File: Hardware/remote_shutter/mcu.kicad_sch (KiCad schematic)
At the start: 27 parts, among them J4 Buzzer, U2 ESP32-PICO-MINI-02, Y1 NX3215SA-32.768K-STD-MUA-14

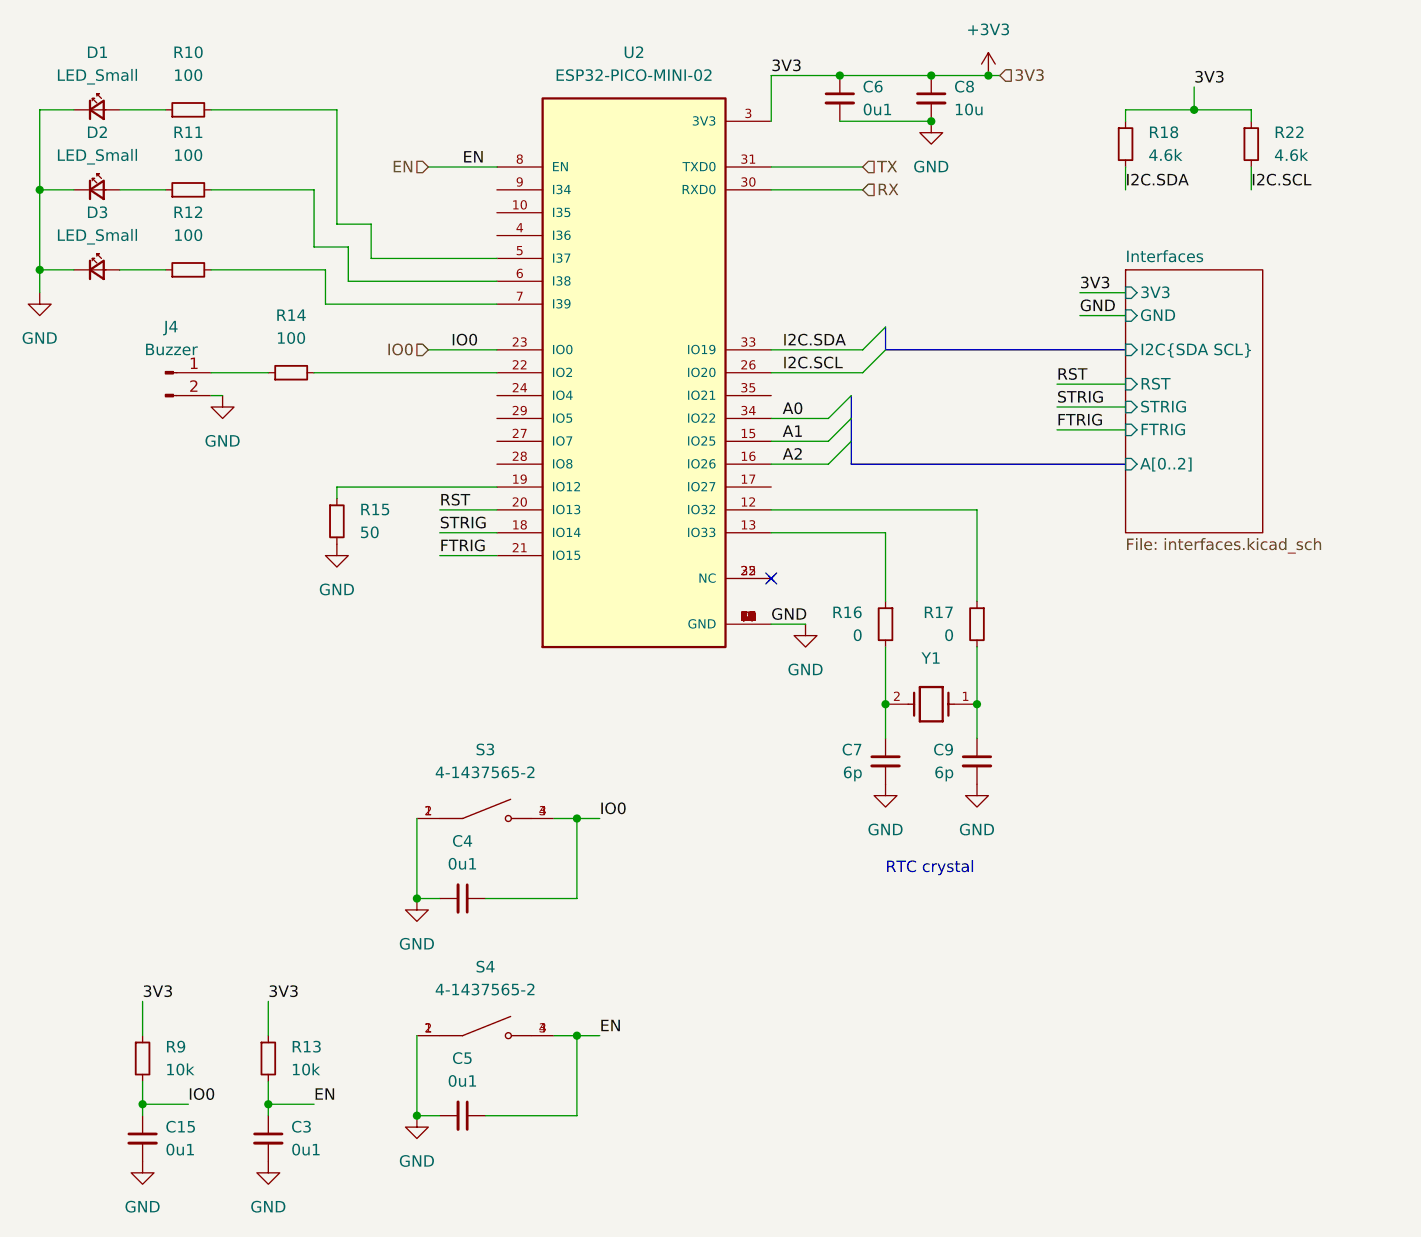
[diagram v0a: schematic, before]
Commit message: Added debug connectors
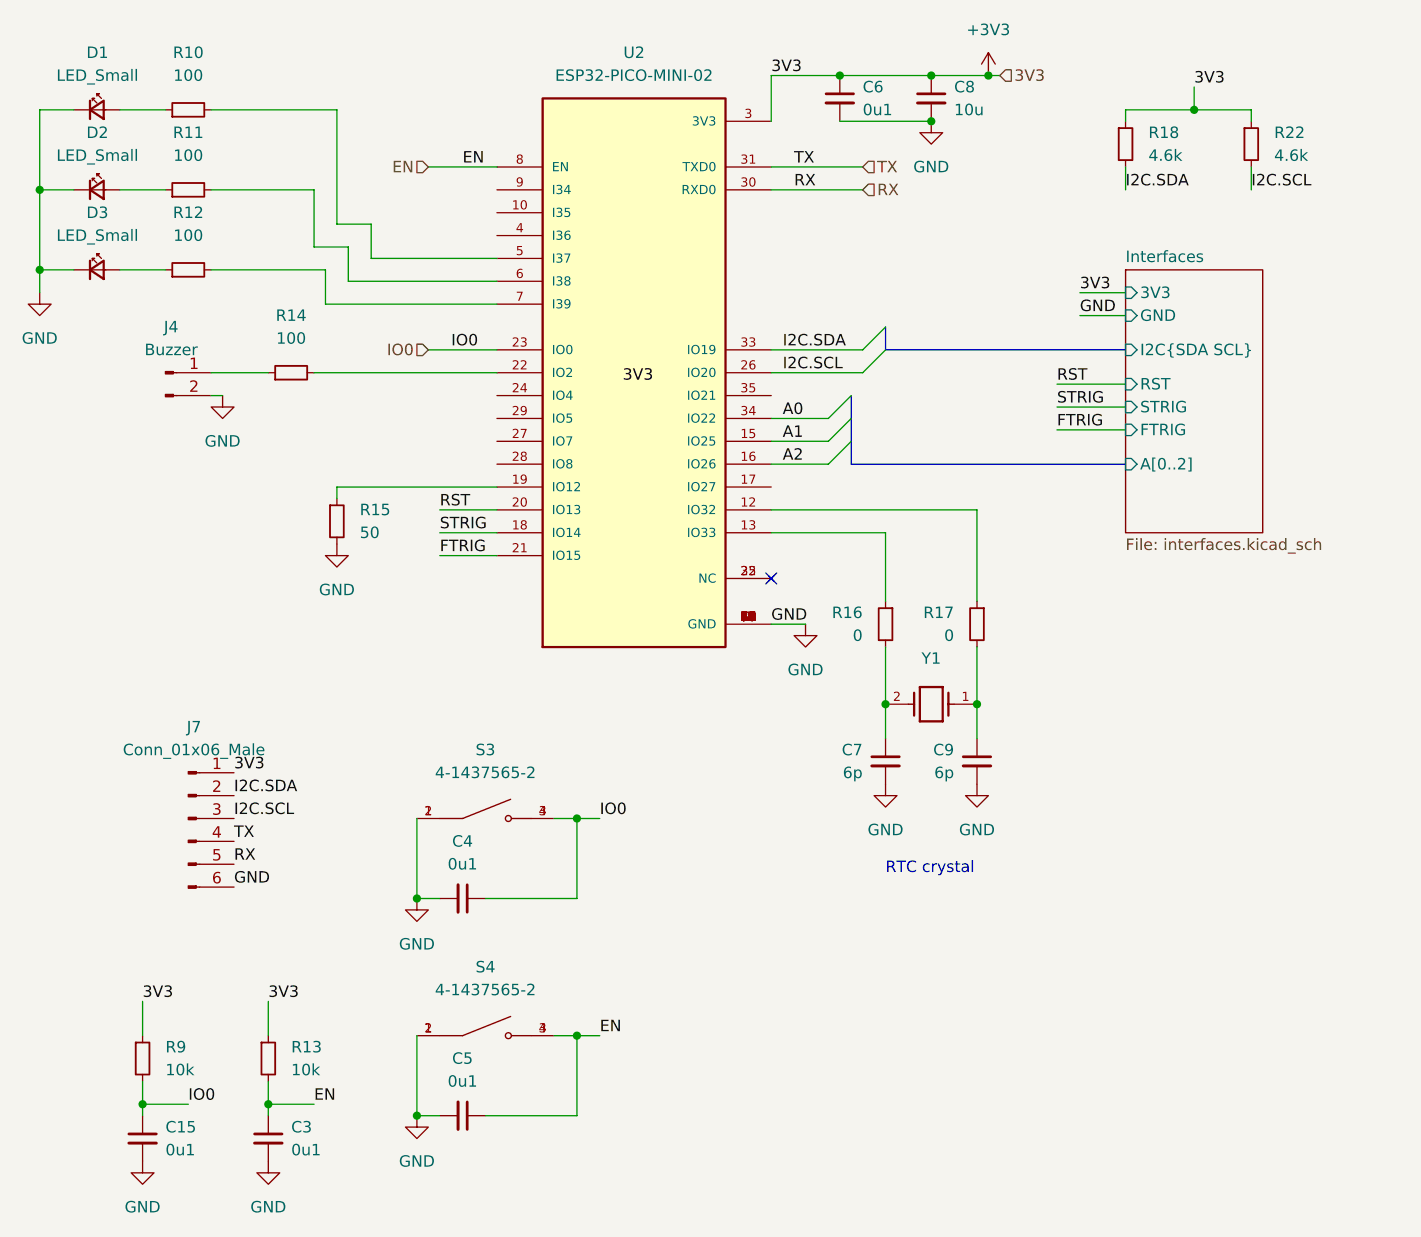
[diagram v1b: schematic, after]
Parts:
- added J7: Conn_01x06_Male, Connector_PinHeader_2.54mm:PinHeader_1x06_P2.54mm_Vertical, symbol Connector:Conn_01x06_Male
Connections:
- net +3V3: now also J7.1 (Pin_1)
- net GND: now also J7.6 (Pin_6)
- net I2C.SCL: now also J7.3 (Pin_3)
- net I2C.SDA: now also J7.2 (Pin_2)
- net RX: now also J7.5 (Pin_5)
- net TX: now also J7.4 (Pin_4)
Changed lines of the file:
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@@
+    (effects (font (size 1.27 1.27)) (justify left bottom))
+  )
+  (label "TX" (at 153.67 55.88 0)
     (effects (font (size 1.27 1.27)) (justify left bottom))
   )
@@
     (effects (font (size 1.27 1.27)) (justify left bottom))
   )
+  (label "GND" (at 91.44 135.89 0)
+    (effects (font (size 1.27 1.27)) (justify left bottom))
+  )
   (label "3V3" (at 95.25 148.59 0)
     (effects (font (size 1.27 1.27)) (justify left bottom))
   )
+  (label "RX" (at 153.67 58.42 0)
+    (effects (font (size 1.27 1.27)) (justify left bottom))
+  )
+  (label "RX" (at 91.44 133.35 0)
+    (effects (font (size 1.27 1.27)) (justify left bottom))
+  )
   (label "EN" (at 132.08 152.4 0)
     (effects (font (size 1.27 1.27)) (justify left bottom))
@@
     (effects (font (size 1.27 1.27)) (justify left bottom))
   )
+  (label "3V3" (at 91.44 123.19 0)
+    (effects (font (size 1.27 1.27)) (justify left bottom))
+  )
   (label "RST" (at 114.3 93.98 0)
     (effects (font (size 1.27 1.27)) (justify left bottom))
@@
     (effects (font (size 1.27 1.27)) (justify left bottom))
   )
+  (label "TX" (at 91.44 130.81 0)
+    (effects (font (size 1.27 1.27)) (justify left bottom))
+  )
   (label "FTRIG" (at 114.3 99.06 0)
     (effects (font (size 1.27 1.27)) (justify left bottom))
@@
     (effects (font (size 1.27 1.27)) (justify left bottom))
   )
+  (label "I2C.SCL" (at 91.44 128.27 0)
+    (effects (font (size 1.27 1.27)) (justify left bottom))
+  )
   (label "I2C.SCL" (at 204.47 58.42 0)
     (effects (font (size 1.27 1.27)) (justify left bottom))
   )
+  (label "I2C.SDA" (at 91.44 125.73 0)
+    (effects (font (size 1.27 1.27)) (justify left bottom))
+  )
   (label "STRIG" (at 182.88 82.55 0)
     (effects (font (size 1.27 1.27)) (justify left bottom))
@@
   )
   (label "IO0" (at 86.36 160.02 0)
+    (effects (font (size 1.27 1.27)) (justify left bottom))
+  )
+  (label "3V3" (at 134.62 80.01 0)
     (effects (font (size 1.27 1.27)) (justify left bottom))
   )
@@
     (pin "2")
   )
+  (symbol (lib_id "Connector:Conn_01x06_Male") (at 86.36 128.27 0) (unit 1)
+    (in_bom yes) (on_board yes) (fields_autoplaced)
+    (property "Reference" "J7" (id 0) (at 86.995 118.11 0))
+    (property "Value" "Conn_01x06_Male" (id 1) (at 86.995 120.65 0))
+    (property "Footprint" "Connector_PinHeader_2.54mm:PinHeader_1x06_P2.54mm_Vertical" (id 2) (at 86.36 128.27 0)
+      (effects (font (size 1.27 1.27)) hide)
+    )
+    (property "Datasheet" "~" (id 3) (at 86.36 128.27 0)
+      (effects (font (size 1.27 1.27)) hide)
+    )
+    (pin "1")
+    (pin "2")
+    (pin "3")
+    (pin "4")
+    (pin "5")
+    (pin "6")
+  )
   (symbol (lib_id "Device:LED_Small") (at 76.2 58.42 0) (unit 1)
